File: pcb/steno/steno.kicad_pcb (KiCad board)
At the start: 2 copper layers, 270.1 x 95.3 mm, 85 parts, among them J1 USB_mini_micro_B, K1 SW_Push, K10 SW_Push, K11 SW_Push, K12 SW_Push, K13 SW_Push, K14 SW_Push, K15 SW_Push, K16 SW_Push, K17 SW_Push, K18 SW_Push, K19 SW_Push, K2 SW_Push, K20 SW_Push, K21 SW_Push, K22 SW_Push, K23 SW_Push, K24 SW_Push, K25 SW_Push, K26 SW_Push, K27 SW_Push, K28 SW_Push, K29 SW_Push, K3 SW_Push, K30 SW_Push, K4 SW_Push, K5 SW_Push, K6 SW_Push, K7 SW_Push, K8 SW_Push, K9 SW_Push, SW1 SW_Push, U1 ATmega32U4-AU, U2 MT25QL128ABA1ESE, U3 MCP1700-3302E_SOT23, U4 LCD2.2in, U5 4050, Y1 16MHz

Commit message: [PCB] Use "raw" LCD + backside components
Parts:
- added DICT: SW_Push, Button_Switch_SMD:SW_SPST_B3U-1000P, F.Cu at (139.8, 70.4)
- added R10: 220, Resistor_SMD:R_0603_1608Metric, B.Cu at (156.5, 119.5)
- added R6: 10k, Resistor_SMD:R_0805_2012Metric, F.Cu at (140.8, 74.9)
- added R7: 220, Resistor_SMD:R_0603_1608Metric, B.Cu at (156.5, 124.0)
- added R8: 220, Resistor_SMD:R_0603_1608Metric, B.Cu at (156.5, 122.5)
- added R9: 220, Resistor_SMD:R_0603_1608Metric, B.Cu at (156.5, 121.0)
- C1, C10, C2, C3, C4, C5, C6, C7, C8, C9, F1, R4, R5, U1, U2, U3, U5, Y1: moved to B.Cu
- R2, R3: value 22 -> 22; moved to B.Cu
- moved C10 34.7 mm to (131.1, 93.2), turned to 90 degrees
- moved C9 31.1 mm to (134.6, 90.2)
- moved U3 31.1 mm to (134.6, 93.2)
- moved C2 30.7 mm to (160.3, 85.2), turned to 180 degrees
- moved Y1 30.6 mm to (160.6, 90.7)
- moved C1 30.4 mm to (160.6, 96.2), turned to 0 degrees
- moved C8 29.2 mm to (151.6, 80.2), turned to 180 degrees
- moved R4 26.7 mm to (134.6, 96.2), turned to 0 degrees
- moved C5 22.7 mm to (156.1, 88.7)
- moved R5 22.0 mm to (141.8, 109.4), turned to 90 degrees
- moved C3 20.9 mm to (137.6, 92.2), turned to 90 degrees
- moved C7 19.8 mm to (139.3, 94.9), turned to 270 degrees
- moved U2 17.2 mm to (147.8, 110.4), turned to 180 degrees
- moved C4 16.1 mm to (148.0, 80.0), turned to 180 degrees
- moved U5 16.0 mm to (135.3, 112.9), turned to 270 degrees
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- renumbered SW1 to RESET
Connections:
- net Net-(R1-Pad1) renamed RESET
- U1 pad 19: ROW1 -> ROW4
- U1 pad 20: ROW2 -> ROW5
- U1 pad 25: Net-(U1-Pad25) -> C\D
- U1 pad 26: Net-(U1-Pad26) -> LCD_CS
- U1 pad 37: LCD_CS -> Net-(U1-Pad37)
- U1 pad 38: LCD_RST -> Net-(U1-Pad38)
- U1 pad 39: C\D -> Net-(U1-Pad39)
- U1 pad 40: ROW5 -> ROW2
- U1 pad 41: ROW4 -> ROW1
- U4 pad 10: LITE_3V3 -> +3V3
- U4 pad 2: +5V -> Net-(U4-Pad2)
- U4 pad 3: C\D -> SCLK_3V3
- U4 pad 4: LCD_RST -> C\D_3V3
- U4 pad 5: Net-(U4-Pad5) -> LCD_CS_3V3
- U4 pad 6: LCD_CS -> MOSI_3V3
- U4 pad 7: MOSI_3V3 -> MISO
- U4 pad 8: MISO -> GND
- U4 pad 9: SCLK_3V3 -> +3V3
- U5 pad 10: LITE_3V3 -> Net-(U5-Pad10)
- U5 pad 11: (no net) -> C\D
- U5 pad 12: (no net) -> C\D_3V3
- U5 pad 14: (no net) -> LCD_CS
- U5 pad 15: (no net) -> LCD_CS_3V3
- U5 pad 2: MOSI_3V3 -> SCLK_3V3
- U5 pad 3: MOSI_5V -> SCLK_5V
- U5 pad 4: SCLK_3V3 -> MOSI_3V3
- U5 pad 5: SCLK_5V -> MOSI_5V
- U5 pad 9: LITE_5V -> Net-(U5-Pad9)
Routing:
- net +5V: track 124.0 -> 75.3 mm, vias 8 -> 2
- net LCD_RST: track 43.6 -> 0.00 mm, vias 1 -> 0
- net +3V3: track 32.3 -> 69.9 mm, vias 0 -> 2
- net GND: track 102.6 -> 81.1 mm, vias 16 -> 25
- net LCD_CS_3V3: track 0.00 -> 20.9 mm
- net LITE_5V: track 20.2 -> 0.00 mm
- net ROW3: track 147.7 -> 167.3 mm, vias 1 -> 0
- net ROW1: track 157.0 -> 137.8 mm
- net Net-(R6-Pad2): track 0.00 -> 19.2 mm, vias 0 -> 1
- net RESET: track 35.1 -> 17.8 mm, vias 0 -> 1
- net C\D_3V3: track 0.00 -> 16.5 mm
- net ROW4: track 154.6 -> 138.7 mm, vias 0 -> 1
- net COL4: track 239.1 -> 225.4 mm
- net COL3: track 271.4 -> 257.8 mm
- net ROW2: track 144.2 -> 131.3 mm
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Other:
- board size 270.1 x 95.3 mm -> 264.6 x 94.5 mm
- board text added: "Open sourced @ github.com/crides/steno"
- board text removed: "Part of a senior project @ UIUC ECE 445 By: - Haoqing "Steven" Zhu - Rishi Krishnan - Soham Karanjikar Open sourced @ github.com/crides/steno"

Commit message: [PCB] normalize stagger + compacting
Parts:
- C5, C6, C7: value 0.1uF -> 104
- R1, R6: moved to B.Cu
- moved C7 15.8 mm to (131.5, 81.1)
- moved C3 15.8 mm to (131.3, 77.7)
- moved C6 14.9 mm to (145.0, 85.6)
- moved C5 14.9 mm to (149.8, 75.1)
- moved U5 14.9 mm to (129.0, 99.3)
- moved C1 14.9 mm to (154.3, 82.6)
- moved R4 14.9 mm to (128.3, 82.6)
- moved U4 14.9 mm to (140.5, 92.3)
- moved U3 14.9 mm to (128.3, 79.6)
- moved R9 14.9 mm to (150.2, 107.4)
- moved R5 14.9 mm to (135.5, 95.8)
- moved Y1 14.9 mm to (154.3, 77.1)
- moved R7 14.9 mm to (150.2, 110.4)
- moved R8 14.9 mm to (150.2, 108.9)
- moved C2 14.9 mm to (154.1, 71.6)
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- renumbered U2 to MT25Q
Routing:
- net COL3: track 257.8 -> 278.3 mm
- net ROW4: track 138.7 -> 120.9 mm
- net ROW1: track 137.8 -> 120.1 mm
- net ROW5: track 139.5 -> 122.8 mm
- net ROW2: track 131.3 -> 123.2 mm
- net +5V: track 75.3 -> 67.8 mm, vias 2 -> 0
- net COL1: track 325.0 -> 330.7 mm
- net GND: track 81.1 -> 75.8 mm, vias 25 -> 21
- net COL2: track 289.3 -> 293.9 mm
- net RESET: track 17.8 -> 13.3 mm
- net Net-(R2-Pad1): track 7.98 -> 3.65 mm
- net COL6: track 145.8 -> 150.0 mm
- net Net-(R3-Pad1): track 7.69 -> 3.94 mm
- net ROW3: track 167.3 -> 163.7 mm
- net COL5: track 183.1 -> 185.7 mm
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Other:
- board size 264.6 x 94.5 mm -> 259.9 x 85.6 mm

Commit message: [PCB] Use new PG1350 footprint + remove unneeded libraries
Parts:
- removed D1, D10, D11, D12, D13, D14, D15, D16, D17, D18, D19, D2, D20, D21, D22, D23, D24, D25, D26, D27, D28, D29, D3, D30, D4, D5, D6, D7, D8, D9: DIODE, Diode_SMD:D_SOD-123
- K1, K10, K11, K12, K13, K14, K15, K16, K17, K18, K19, K2, K20, K21, K22, K23, K24, K25, K26, K27, K28, K29, K3, K30, K4, K5, K6, K7, K8, K9: value SW_Push -> PG1350; footprint Keebio-Parts:Kailh-PG1350-1u-No-Clickhole -> pg1350:PG1350
- Y1: footprint Crystal:Crystal_SMD_EuroQuartz_MJ-4Pin_5.0x3.2mm_HandSoldering -> Crystal:Crystal_SMD_EuroQuartz_MJ-4Pin_5.0x3.2mm
- moved K12 4.53 mm to (107.9, 95.2), turned to 350 degrees
- moved K9 4.53 mm to (54.8, 85.8), turned to 350 degrees
- moved K10 4.53 mm to (73.0, 86.0), turned to 350 degrees
- moved K6 4.53 mm to (110.9, 78.4), turned to 350 degrees
- moved K1 4.53 mm to (21.4, 67.7), turned to 350 degrees
- moved K11 4.53 mm to (90.2, 92.1), turned to 350 degrees
- moved K3 4.53 mm to (57.7, 69.1), turned to 350 degrees
- moved K8 4.53 mm to (36.2, 87.6), turned to 350 degrees
- moved K4 4.53 mm to (76.0, 69.2), turned to 350 degrees
- moved K7 4.53 mm to (18.4, 84.5), turned to 350 degrees
- moved K2 4.53 mm to (39.1, 70.9), turned to 350 degrees
- moved K13 4.53 mm to (79.8, 125.2), turned to 350 degrees
- moved K14 4.53 mm to (97.5, 128.4), turned to 350 degrees
- moved K15 4.53 mm to (115.2, 131.5), turned to 350 degrees
- moved K29 4.50 mm to (190.6, 92.1), turned to 10 degrees
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- renumbered RESET to SW1, DICT to SW2, MT25Q to U2
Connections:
- K1 pad 2: Net-(D1-Pad1) -> COL1
- K10 pad 2: Net-(D10-Pad1) -> COL4
- K11 pad 2: Net-(D11-Pad1) -> COL5
- K12 pad 2: Net-(D12-Pad1) -> COL6
- K13 pad 2: Net-(D13-Pad1) -> COL1
- K14 pad 2: Net-(D14-Pad1) -> COL2
- K15 pad 2: Net-(D15-Pad1) -> COL3
- K16 pad 2: Net-(D16-Pad1) -> COL4
- K17 pad 2: Net-(D17-Pad1) -> COL5
- K18 pad 2: Net-(D18-Pad1) -> COL6
- K19 pad 2: Net-(D19-Pad1) -> COL1
- K2 pad 2: Net-(D2-Pad1) -> COL2
- K20 pad 2: Net-(D20-Pad1) -> COL2
- K21 pad 2: Net-(D21-Pad1) -> COL3
- K22 pad 2: Net-(D22-Pad1) -> COL4
- K23 pad 2: Net-(D23-Pad1) -> COL5
- K24 pad 2: Net-(D24-Pad1) -> COL6
- K25 pad 2: Net-(D25-Pad1) -> COL1
- K26 pad 2: Net-(D26-Pad1) -> COL2
- K27 pad 2: Net-(D27-Pad1) -> COL3
- K28 pad 2: Net-(D28-Pad1) -> COL4
- K29 pad 2: Net-(D29-Pad1) -> COL5
- K3 pad 2: Net-(D3-Pad1) -> COL3
- K30 pad 2: Net-(D30-Pad1) -> COL6
- K4 pad 2: Net-(D4-Pad1) -> COL4
- K5 pad 2: Net-(D5-Pad1) -> COL5
- K6 pad 2: Net-(D6-Pad1) -> COL6
- K7 pad 2: Net-(D7-Pad1) -> COL1
- K8 pad 2: Net-(D8-Pad1) -> COL2
- K9 pad 2: Net-(D9-Pad1) -> COL3
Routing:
- net COL3: track 278.3 -> 261.3 mm
- net Net-(D16-Pad1): track 9.69 -> 0.00 mm
- net Net-(D27-Pad1): track 9.69 -> 0.00 mm
- net Net-(D18-Pad1): track 9.69 -> 0.00 mm
- net Net-(D28-Pad1): track 9.69 -> 0.00 mm
- net Net-(D22-Pad1): track 9.69 -> 0.00 mm
- net Net-(D29-Pad1): track 9.69 -> 0.00 mm
- net Net-(D20-Pad1): track 9.69 -> 0.00 mm
- net Net-(D30-Pad1): track 9.69 -> 0.00 mm
- net Net-(D17-Pad1): track 9.69 -> 0.00 mm
- net Net-(D25-Pad1): track 9.69 -> 0.00 mm
- net Net-(D26-Pad1): track 9.69 -> 0.00 mm
- net Net-(D24-Pad1): track 9.69 -> 0.00 mm
- net Net-(D19-Pad1): track 9.69 -> 0.00 mm
- net Net-(D23-Pad1): track 9.69 -> 0.00 mm
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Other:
- board size 259.9 x 85.6 mm -> 259.5 x 85.1 mm
- board text added: "Public test #1"
- board text removed: "JLCJLCJLCJLC"

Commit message: [PCB] Change to USB-C connector + protection diode
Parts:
- added R11: 5.1k, Resistor_SMD:R_0603_1608Metric, B.Cu at (144.2, 65.7)
- added R12: 5.1k, Resistor_SMD:R_0603_1608Metric, B.Cu at (138.2, 65.7)
- added U6: SRV05-4, Package_TO_SOT_SMD:SOT-23-6, B.Cu at (141.1, 66.3)
- J1: value USB_mini_micro_B -> USB_C_Receptacle_USB2.0; footprint Connector_USB:AMPHENOL_10118192-0001LF -> Connector_USB:USB_C_Receptacle_HRO_TYPE-C-31-M-12
- Y1: footprint Crystal:Crystal_SMD_EuroQuartz_MJ-4Pin_5.0x3.2mm -> Crystal:Crystal_SMD_EuroQuartz_MT-4Pin_3.2x2.5mm
- moved J1 5.96 mm to (140.4, 57.1)
- moved R6 5.08 mm to (135.3, 73.6)
- moved SW2 2.86 mm to (133.1, 58.2)
- moved SW1 2.86 mm to (147.6, 58.2)
- moved C2 2.61 mm to (155.7, 75.1)
- moved R2 2.50 mm to (141.8, 70.1)
- moved R3 2.50 mm to (140.4, 70.1)
- moved C4 2.38 mm to (144.9, 68.7), turned to 0 degrees
- moved C8 2.24 mm to (150.4, 70.8), turned to 0 degrees
- moved C7 1.01 mm to (133.8, 82.1)
- moved C10 1.01 mm to (127.6, 80.5)
- moved C5 1.01 mm to (151.3, 76.1)
- moved C3 1.00 mm to (133.6, 78.7)
- moved C6 1.00 mm to (147.3, 86.6)
- moved C9 1.00 mm to (130.6, 77.6)
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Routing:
- net Net-(J1-PadS1): track 0.00 -> 17.0 mm
- net VCC: track 6.89 -> 20.2 mm, vias 1 -> 2
- net D+: track 4.27 -> 13.4 mm
- net D-: track 4.11 -> 11.4 mm
- net Net-(R6-Pad2): track 18.4 -> 25.7 mm
- net +5V: track 68.0 -> 61.5 mm, vias 2 -> 0
- net GND: track 75.6 -> 69.7 mm, vias 23 -> 27
- net Net-(J1-PadA5): track 0.00 -> 5.39 mm, vias 0 -> 1
- net Net-(J1-PadB5): track 0.00 -> 4.10 mm, vias 0 -> 1
- net RESET: track 14.5 -> 18.0 mm
- net Net-(C2-Pad1): track 12.3 -> 10.4 mm
- net Net-(R3-Pad1): track 3.69 -> 2.19 mm
- net Net-(R2-Pad1): track 3.68 -> 2.18 mm
- net Net-(C1-Pad1): track 9.20 -> 8.20 mm
- net SCLK_5V: track 36.9 -> 35.9 mm
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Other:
- outline, holes or cut-outs redrawn
- board text added: "JLCJLCJLCJLC"

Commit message: [PCB] Public test version
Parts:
- removed R1, R6: 10k, Resistor_SMD:R_0805_2012Metric
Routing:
- net Net-(SW2-Pad2): track 25.7 -> 20.5 mm, vias 2 -> 1

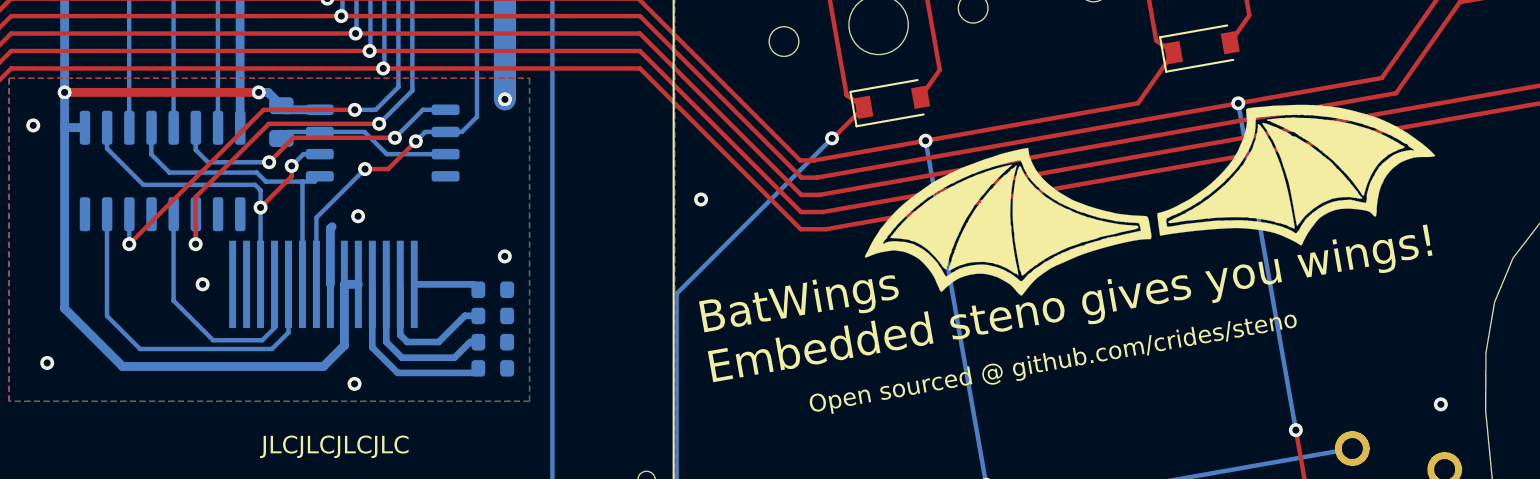
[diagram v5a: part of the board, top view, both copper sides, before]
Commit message: [compiler] Add compiled simple rules
- Remove word list cuz we can't use that anywhere
- Compile simple rules (exception from regex rules) into 64KiB sized binary hashmap
- Rules comes from https://github.com/nimble0/dotterel/blob/master/app/src/main/assets/orthography/english.simple.json
- Load rules at `0xF30000`
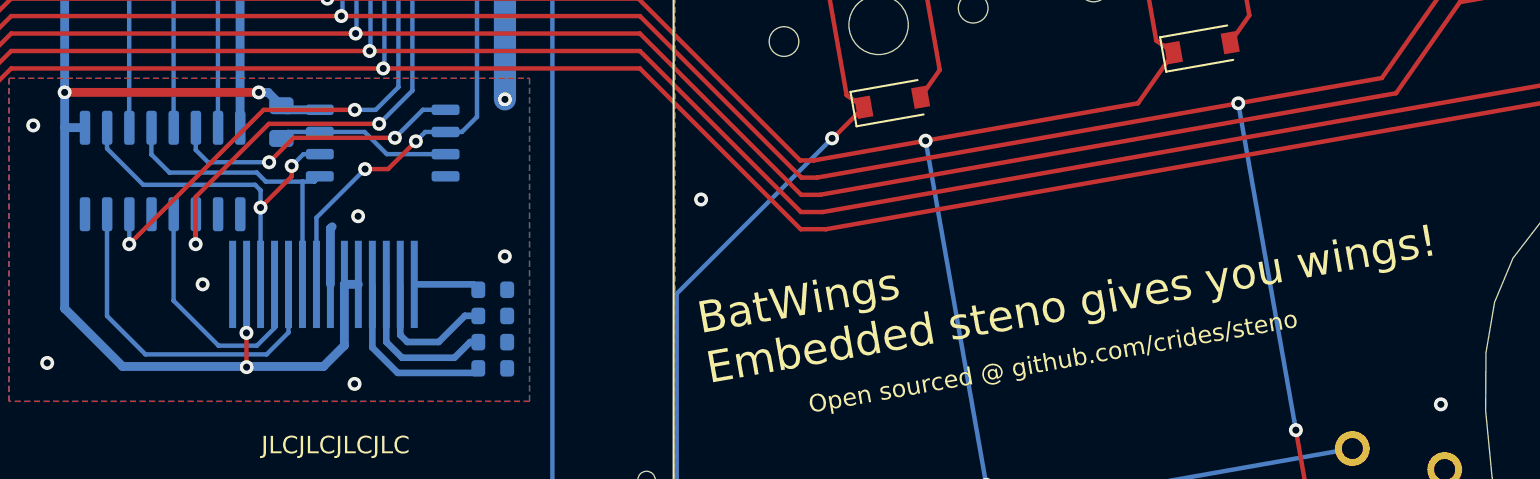
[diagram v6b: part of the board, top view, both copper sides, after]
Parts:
- removed G***: LOGO, misc:batwings
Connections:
- U4 pad 2: Net-(U4-Pad2) -> +3V3
- U5 pad 10: Net-(U5-Pad10) -> (no net)
- U5 pad 9: Net-(U5-Pad9) -> (no net)
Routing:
- net +3V3: track 68.9 -> 73.7 mm, vias 2 -> 4
